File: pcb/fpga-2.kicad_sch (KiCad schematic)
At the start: 7 parts, among them U7 XC7A100T-FGG484

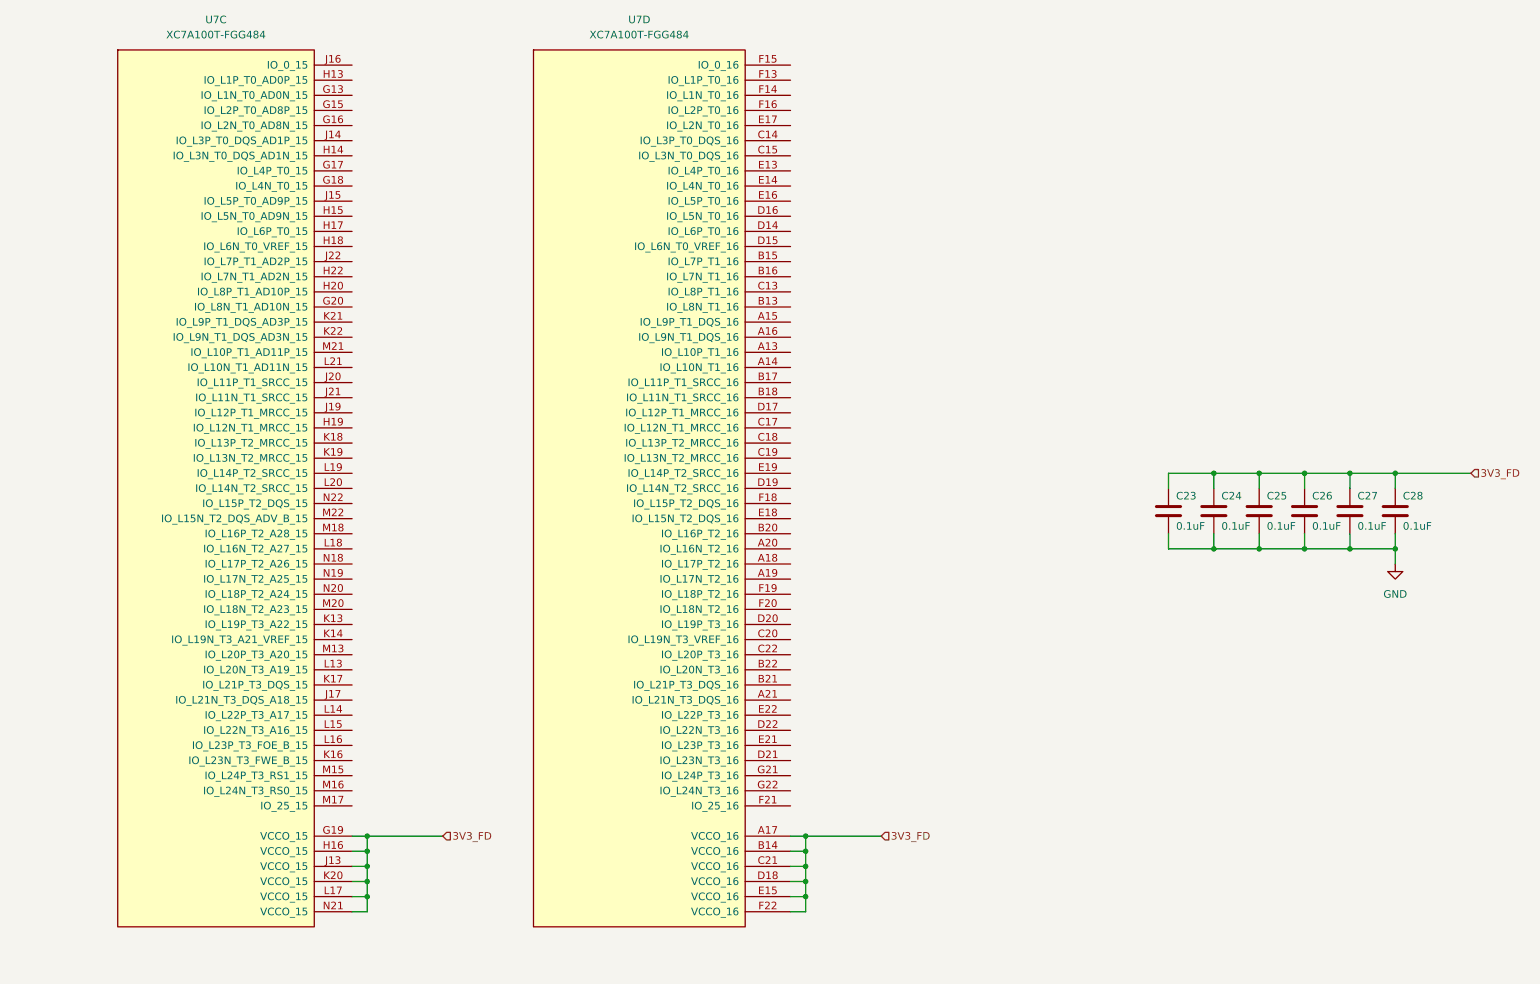
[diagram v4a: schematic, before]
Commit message: restructured power, power plane layout
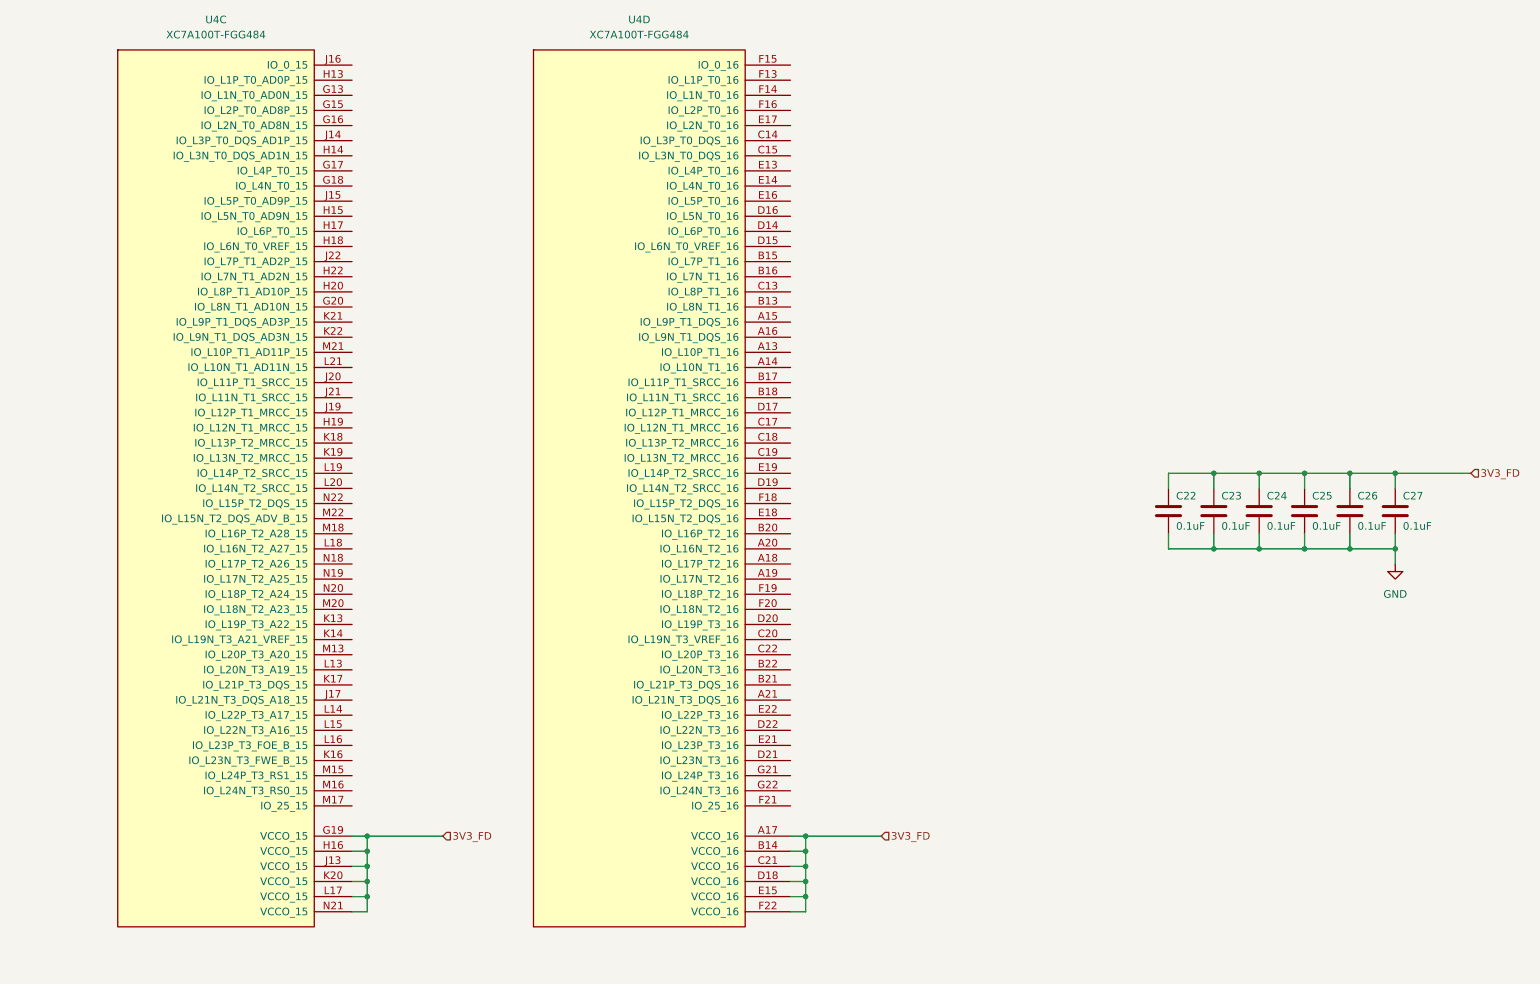
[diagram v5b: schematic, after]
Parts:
- renumbered C23 to C22, C24 to C23, C25 to C24, C26 to C25, C27 to C26, C28 to C27, U7 to U4
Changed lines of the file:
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@@
 		(dnp no)
 		(fields_autoplaced yes)
-		(property "Reference" "U7"
+		(property "Reference" "U4"
 			(at 127 17.78 0)
 			(effects
@@
 			(project "RPi-HwAB-1"
 				(path "/e63e39d7-6ac0-4ffd-8aa3-1841a4541b55/59d21473-a004-4514-8090-fd93db818925/ef42fd34-c1d8-421f-b8cb-1078e483aec9"
-					(reference "U7")
+					(reference "U4")
 					(unit 4)
 				)
@@
 		(on_board yes)
 		(dnp no)
-		(property "Reference" "C26"
+		(property "Reference" "C25"
 			(at 240.03 97.79 0)
 			(effects
@@
 			(project "RPi-HwAB-1"
 				(path "/e63e39d7-6ac0-4ffd-8aa3-1841a4541b55/59d21473-a004-4514-8090-fd93db818925/ef42fd34-c1d8-421f-b8cb-1078e483aec9"
-					(reference "C26")
+					(reference "C25")
 					(unit 1)
 				)
@@
 		(on_board yes)
 		(dnp no)
-		(property "Reference" "C27"
+		(property "Reference" "C26"
 			(at 247.65 97.79 0)
 			(effects
@@
 			(project "RPi-HwAB-1"
 				(path "/e63e39d7-6ac0-4ffd-8aa3-1841a4541b55/59d21473-a004-4514-8090-fd93db818925/ef42fd34-c1d8-421f-b8cb-1078e483aec9"
-					(reference "C27")
+					(reference "C26")
 					(unit 1)
 				)
@@
 		(on_board yes)
 		(dnp no)
-		(property "Reference" "C23"
+		(property "Reference" "C22"
 			(at 217.17 97.79 0)
 			(effects
@@
 			(project "RPi-HwAB-1"
 				(path "/e63e39d7-6ac0-4ffd-8aa3-1841a4541b55/59d21473-a004-4514-8090-fd93db818925/ef42fd34-c1d8-421f-b8cb-1078e483aec9"
-					(reference "C23")
+					(reference "C22")
 					(unit 1)
 				)
@@
 		(dnp no)
 		(fields_autoplaced yes)
-		(property "Reference" "U7"
+		(property "Reference" "U4"
 			(at 55.88 17.78 0)
 			(effects
@@
 			(project "RPi-HwAB-1"
 				(path "/e63e39d7-6ac0-4ffd-8aa3-1841a4541b55/59d21473-a004-4514-8090-fd93db818925/ef42fd34-c1d8-421f-b8cb-1078e483aec9"
-					(reference "U7")
+					(reference "U4")
 					(unit 3)
 				)
@@
 		(on_board yes)
 		(dnp no)
-		(property "Reference" "C28"
+		(property "Reference" "C27"
 			(at 255.27 97.79 0)
 			(effects
@@
 			(project "RPi-HwAB-1"
 				(path "/e63e39d7-6ac0-4ffd-8aa3-1841a4541b55/59d21473-a004-4514-8090-fd93db818925/ef42fd34-c1d8-421f-b8cb-1078e483aec9"
-					(reference "C28")
+					(reference "C27")
 					(unit 1)
 				)
@@
 		(on_board yes)
 		(dnp no)
-		(property "Reference" "C25"
+		(property "Reference" "C24"
 			(at 232.41 97.79 0)
 			(effects
@@
 			(project "RPi-HwAB-1"
 				(path "/e63e39d7-6ac0-4ffd-8aa3-1841a4541b55/59d21473-a004-4514-8090-fd93db818925/ef42fd34-c1d8-421f-b8cb-1078e483aec9"
-					(reference "C25")
+					(reference "C24")
 					(unit 1)
 				)
@@
 		(dnp no)
 		(fields_autoplaced yes)
-		(property "Reference" "#PWR026"
+		(property "Reference" "#PWR023"
 			(at 254 115.57 0)
 			(effects
@@
 			(project "RPi-HwAB-1"
 				(path "/e63e39d7-6ac0-4ffd-8aa3-1841a4541b55/59d21473-a004-4514-8090-fd93db818925/ef42fd34-c1d8-421f-b8cb-1078e483aec9"
-					(reference "#PWR026")
+					(reference "#PWR023")
 					(unit 1)
 				)
@@
 		(on_board yes)
 		(dnp no)
-		(property "Reference" "C24"
+		(property "Reference" "C23"
 			(at 224.79 97.79 0)
 			(effects
@@
 			(project "RPi-HwAB-1"
 				(path "/e63e39d7-6ac0-4ffd-8aa3-1841a4541b55/59d21473-a004-4514-8090-fd93db818925/ef42fd34-c1d8-421f-b8cb-1078e483aec9"
-					(reference "C24")
+					(reference "C23")
 					(unit 1)
 				)
